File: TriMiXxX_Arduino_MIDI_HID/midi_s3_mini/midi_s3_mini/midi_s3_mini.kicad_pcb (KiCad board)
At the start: 2 copper layers, 98 x 98 mm, 31 parts, among them J1 Power, J10 OneButtonA_TX, J11 OneButtonB_RX, J2 LOOP, J3 PLAY_CUE, J4 UART_PI, J5 TRACK_ENC, J6 TEMPO, J7 JOG, J8 OneButtonB_TX, J9 OneButtonA_RX, U1 LOLIN_S3_Mini

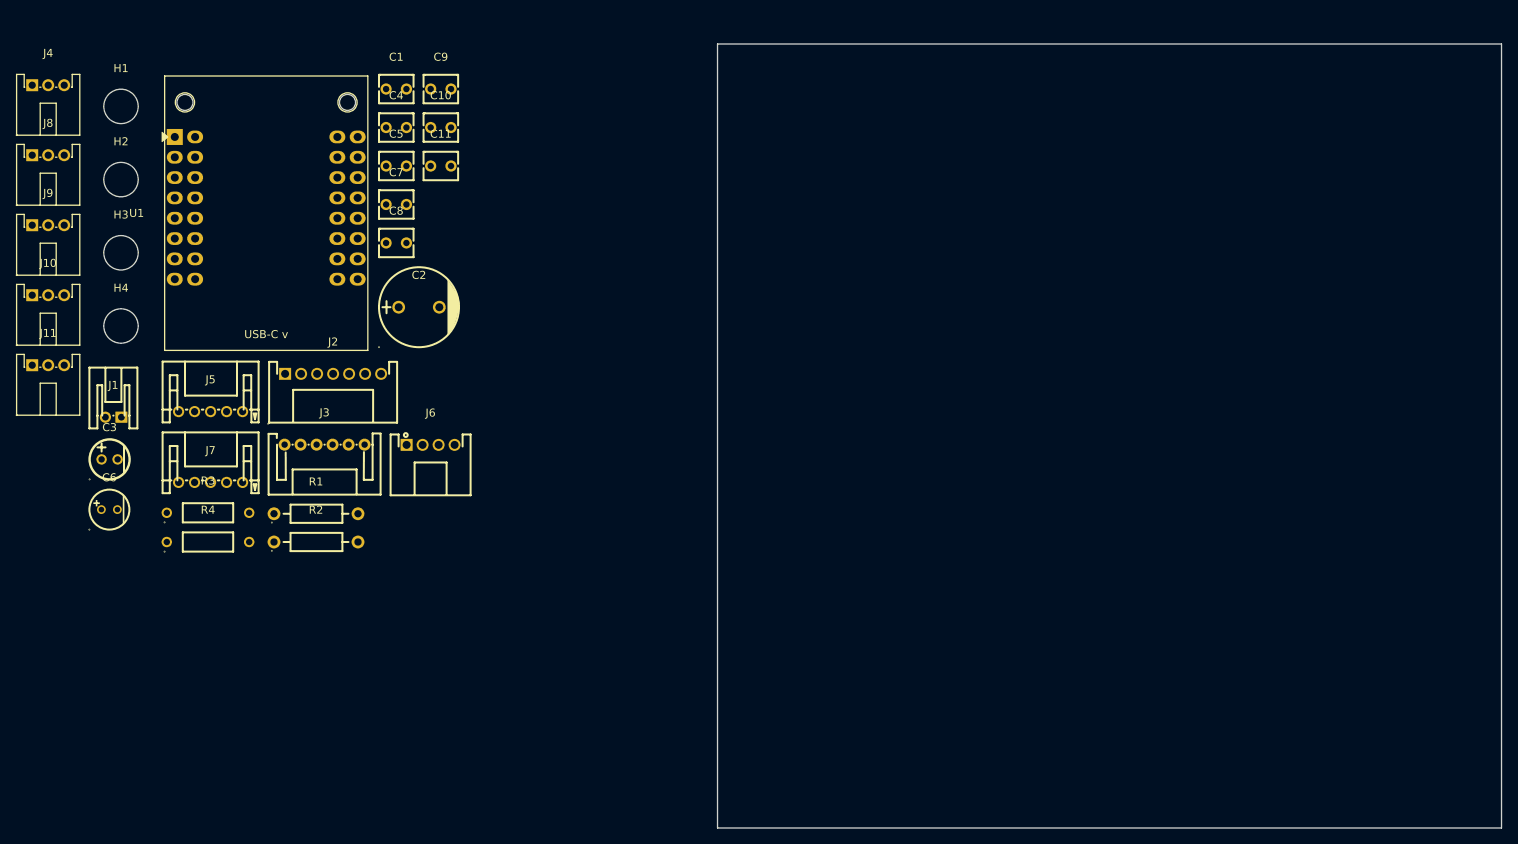
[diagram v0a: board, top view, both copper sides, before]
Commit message: Add Midi S3 Mini board V3
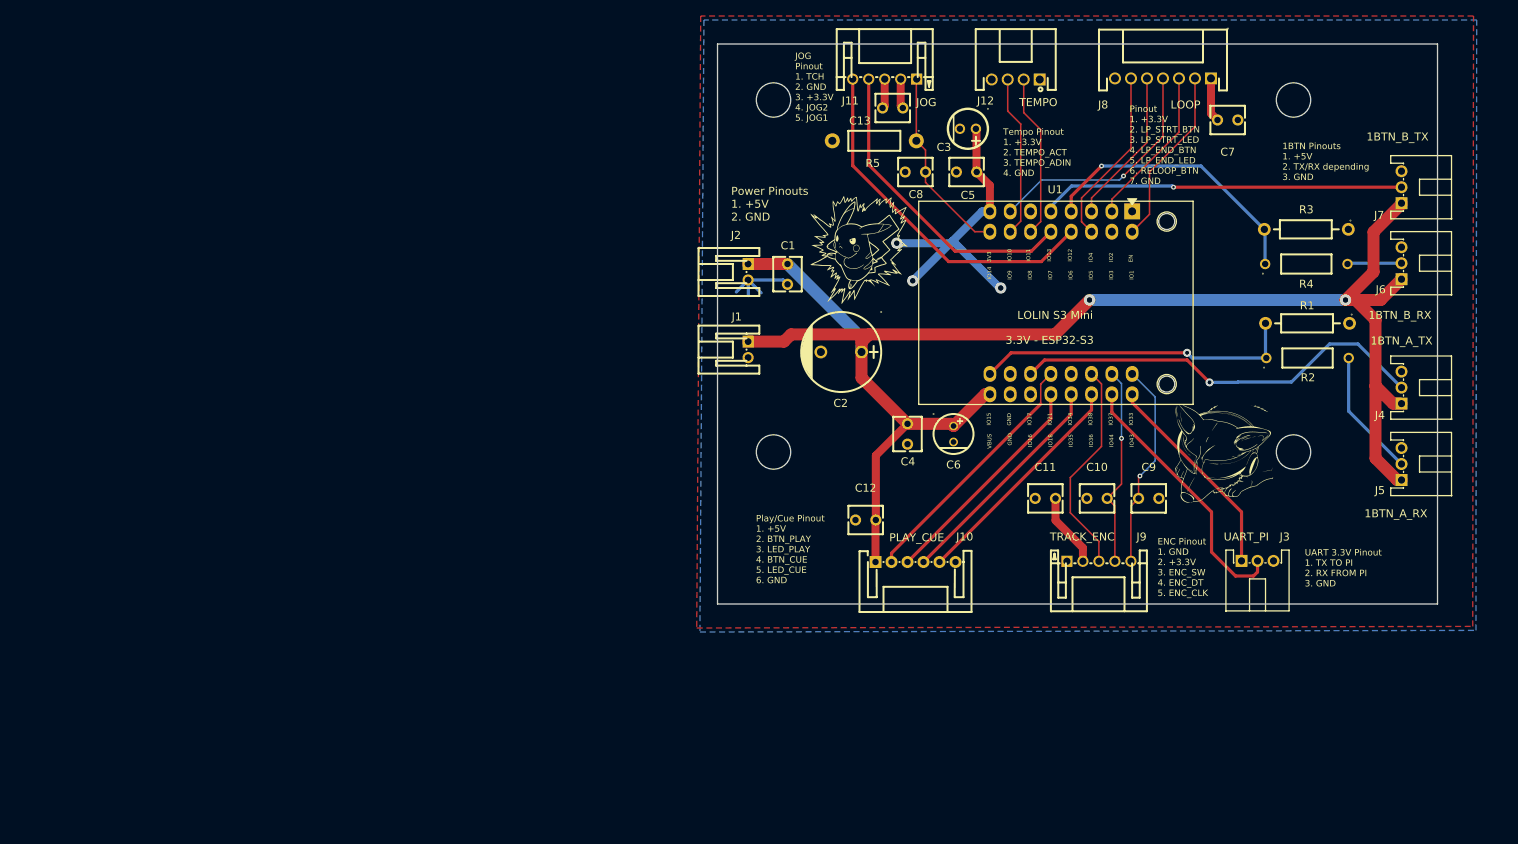
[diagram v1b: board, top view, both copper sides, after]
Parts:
- added C13: 100n, easyeda2kicad:CAP-TH_L4.2-W3.5-P2.54-D0.5, F.Cu at (41.9, 28.0)
- added C8: 100n, easyeda2kicad:CAP-TH_L4.2-W3.5-P2.54-D0.5, F.Cu at (44.7, 36.0)
- added J1: Power2, easyeda2kicad:CONN-TH_S2B-PH-K-S-LF-SN, F.Cu at (23.8, 58.2)
- added R5: 10k, easyeda2kicad:RES-TH_BD2.5-L6.5-P10.50-D0.6, F.Cu at (39.6, 32.1)
- J2: renamed from J1; value Power -> Power1
- J4: renamed from J10; value OneButtonA_TX -> 1BTN_A_TX
- J5: renamed from J9; value OneButtonA_RX -> 1BTN_A_RX
- J6: renamed from J11; value OneButtonB_RX -> 1BTN_B_RX
- J7: renamed from J8; value OneButtonB_TX -> 1BTN_B_TX
- moved J5 171.8 mm to (105.5, 72.5), turned to 90 degrees
- moved J6 169.6 mm to (105.5, 47.4), turned to 90 degrees
- moved J4 169.6 mm to (105.5, 63.0), turned to 90 degrees
- moved J7 169.2 mm to (105.5, 37.9), turned to 90 degrees
- moved J3 162.4 mm to (87.5, 84.6)
- moved H3 148.7 mm to (92.0, 71.0)
- moved H1 146.9 mm to (92.0, 27.0)
- moved R3 141.6 mm to (93.6, 47.5)
- moved R1 138.8 mm to (93.8, 59.2)
- moved R4 129.8 mm to (93.6, 43.2), turned to 180 degrees
- moved U1 129.5 mm to (79.5, 39.7), turned to -90 degrees
- moved R2 126.2 mm to (93.8, 54.9), turned to 180 degrees
- moved C5 115.0 mm to (51.3, 30.6), turned to 180 degrees
- moved J9 112.6 mm to (67.7, 84.7), turned to 180 degrees
- moved J8 110.1 mm to (75.7, 24.3), turned to 180 degrees
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- renumbered C7 to C12, C4 to C3, C8 to C4, C3 to C5, C5 to C7, H2 to H1, H1 to H2, J3 to J10, J7 to J11, J6 to J12, J4 to J3, J2 to J8, J5 to J9, R3 to R1, R1 to R2, R4 to R3, R2 to R4
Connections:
- C11 pad 2: +5V -> +3.3V
- J11 pad 1: GND -> /JOG_TCH
- J11 pad 2: +3.3V -> GND
- J11 pad 3: /JOG1 -> +3.3V
- J11 pad 5: /JOG_TCH -> /JOG1
- J12 pad 1: GND -> +3.3V
- J12 pad 2: +3.3V -> /TEMPO_ADCT
- J12 pad 4: /TEMPO_ADCT -> GND
- J9 pad 3: /ENC_CLK -> /ENC_SW
- J9 pad 5: /ENC_SW -> /ENC_CLK
- U1 pad 14: /TEMPO_ADIN -> /TEMPO_ADCT
- U1 pad 15: /TEMPO_ADCT -> /TEMPO_ADIN
- U1 pad 21: /BTN_CUE -> /BTN_PLAY
- U1 pad 27: /BTN_PLAY -> /LED_CUE
- U1 pad 28: /LED_PLAY -> /BTN_CUE
- U1 pad 29: /LED_CUE -> /LED_PLAY
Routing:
- net +5V: track 0.00 -> 193.9 mm, vias 0 -> 2
- net +3.3V: track 0.00 -> 58.4 mm, vias 0 -> 3
- net /1BTNA_TX: track 0.00 -> 52.5 mm, vias 0 -> 1
- net /1BTNB_TX: track 0.00 -> 45.6 mm, vias 0 -> 1
- net /JOG1: track 0.00 -> 44.6 mm
- net /1BTNA_RX: track 0.00 -> 40.3 mm, vias 0 -> 1
- net /JOG2: track 0.00 -> 39.0 mm
- net /1BTNB_RX: track 0.00 -> 35.2 mm, vias 0 -> 1
- net /UART_RX_FROM_PI: track 0.00 -> 33.5 mm
- net /BTN_PLAY: track 0.00 -> 31.8 mm
- net /LOOP_END_BTN: track 0.00 -> 30.2 mm, vias 0 -> 1
- net /LED_CUE: track 0.00 -> 28.8 mm
- net /BTN_CUE: track 0.00 -> 28.6 mm
- net /LED_PLAY: track 0.00 -> 28.4 mm
- net /ENC_SW: track 0.00 -> 27.3 mm
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- added copper zone on F.Cu, net +3.3V
- added copper zone on B.Cu, net GND
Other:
- board size 98 x 98 mm -> 90 x 70 mm
- board text added: "1BTN Pinouts 1. +5V 2. TX/RX depending 3. GND"
- board text added: "3.3V - ESP32-S3"
- board text added: "ENC Pinout 1. GND 2. +3.3V 3. ENC_SW 4. ENC_DT 5. ENC_CLK"
- board text added: "JOG Pinout 1. TCH 2. GND 3. +3.3V 4. JOG2 5. JOG1"
- board text added: "Pinout 1. +3.3V 2. LP_STRT_BTN 3. LP_STRT_LED 4. LP_END_BTN 5. LP_END_LED 6. RELOOP_BTN 7. GND"
- board text added: "Play/Cue Pinout 1. +5V 2. BTN_PLAY 3. LED_PLAY 4. BTN_CUE 5. LED_CUE 6. GND"
- board text added: "Power Pinouts 1. +5V 2. GND"
- board text added: "Tempo Pinout 1. +3.3V 2. TEMPO_ACT 3. TEMPO_ADIN 4. GND"
- board text added: "TriMiXxX MIDI Control Board V3"
- board text added: "UART 3.3V Pinout 1. TX TO PI 2. RX FROM PI 3. GND"
